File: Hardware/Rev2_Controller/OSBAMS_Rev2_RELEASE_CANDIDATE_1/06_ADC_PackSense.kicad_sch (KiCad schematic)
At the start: 10 parts, among them J6 PACK_SENSE

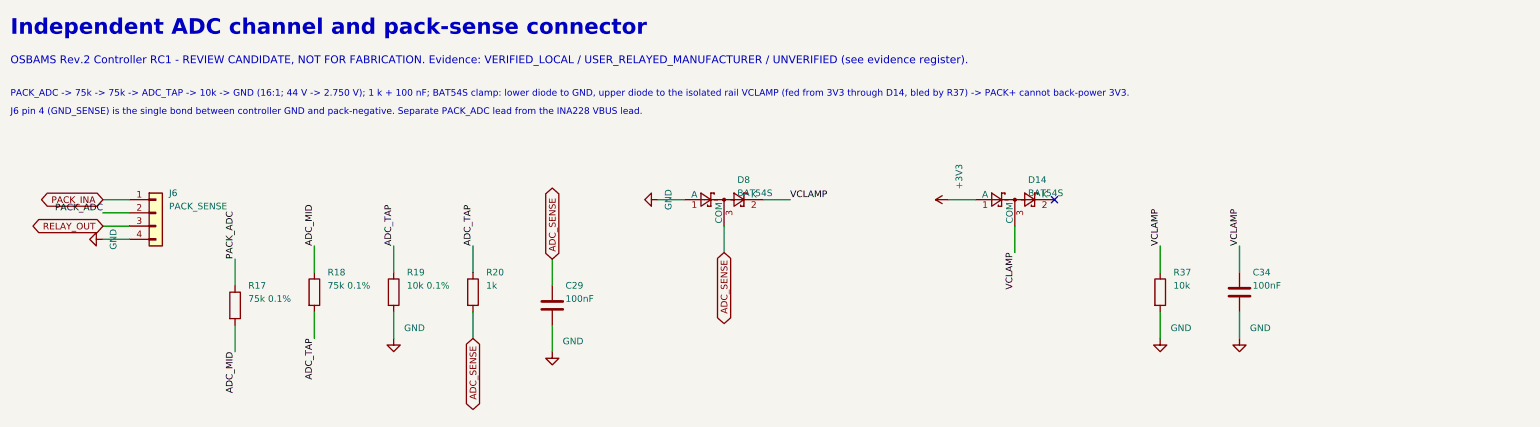
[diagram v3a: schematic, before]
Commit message: RC1.2: pack-sense surge resistors, isolation/clearance rules, buck envelope, evidence classification, no shipped Gerbers
- R41 47R (PACK_INA) and R42/R43 10R (Kelvin lines) upstream of the 1.5SMBJ48A diodes; credible-transient analysis with simulation (PASS)
- custom DRC rules: host-to-controller >= 1.0 mm on every layer, INA228 fine-pitch exemption; pack-level class 0.2 mm (IPC-2221B B4 basis)
- isolation audit per layer with coordinates; XDR 12.0 V / max continuous input 14.4 V; IRLML0060 margin estimate + mandatory first-article checks
- board re-routed: ERC 0, DRC 0, unconnected 0, netlist 0 mismatches (403 pads); silkscreen warnings fixed
- script-generated Gerbers/drills removed from the package; BOM adds qty for 5 boards and MPN suffix status; new evidence-risk, connector-check and pre-PCBWay checklist documents

Co-Authored-By: Claude Sonnet 5.5 <noreply@anthropic.com>
Claude-Session: https://claude.ai/code/session_01HV1TCrYnLTcNjmYdFqCPLo
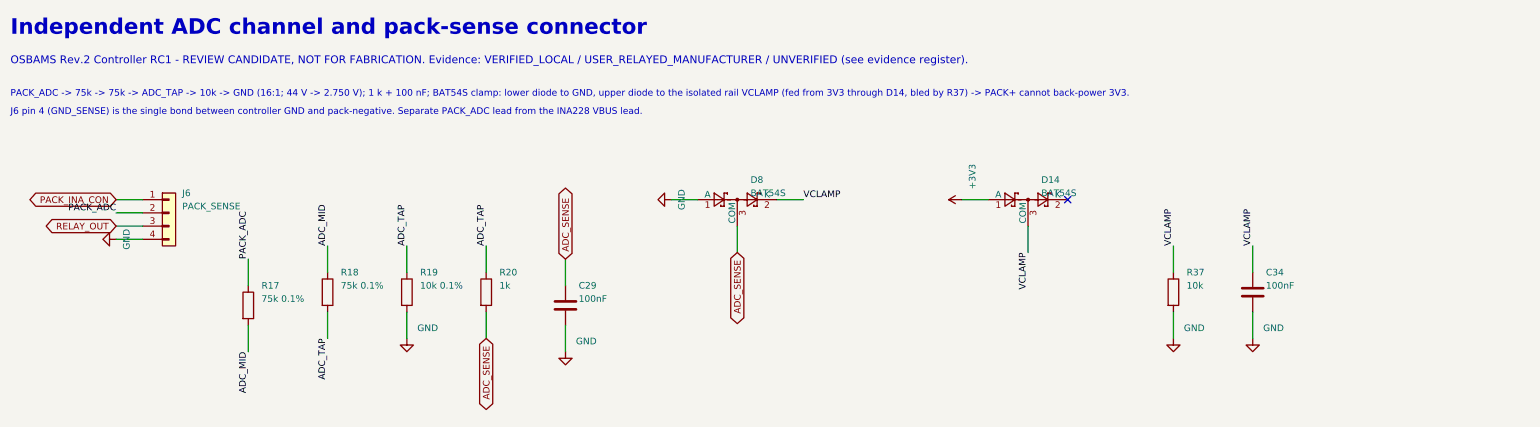
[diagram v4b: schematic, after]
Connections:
- net PACK_INA renamed PACK_INA_CON
